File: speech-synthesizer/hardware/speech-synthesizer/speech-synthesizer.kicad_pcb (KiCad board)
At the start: 2 copper layers, 50.1 x 5.8 mm, 33 parts, among them J1 AudioJack3, Q1 BS250, U1 TMS5220C, U2 ATF22V10C, U3 74HCT245, U4 74HCT374, U5 74HCT374, U6 74HCT74, U7 74HCT688, U8 74HCT688

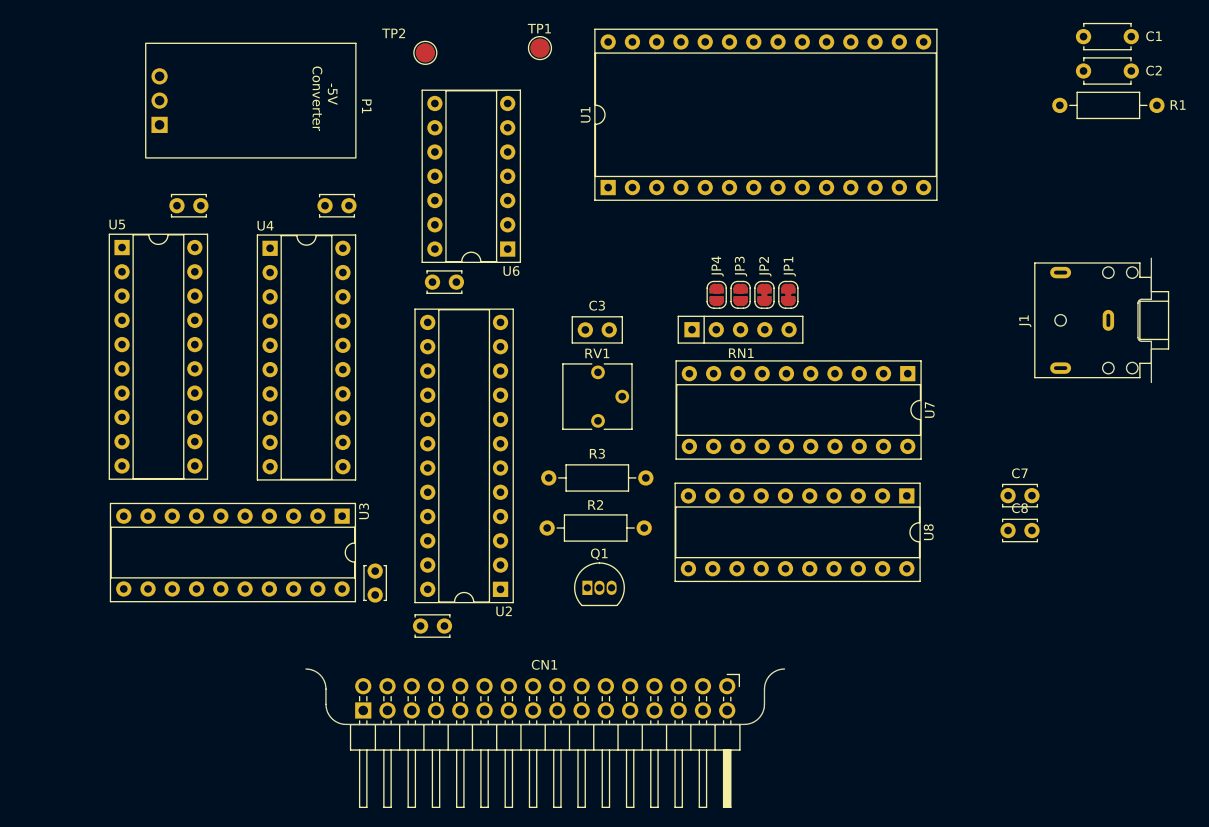
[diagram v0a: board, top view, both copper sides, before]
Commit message: created speech pcb
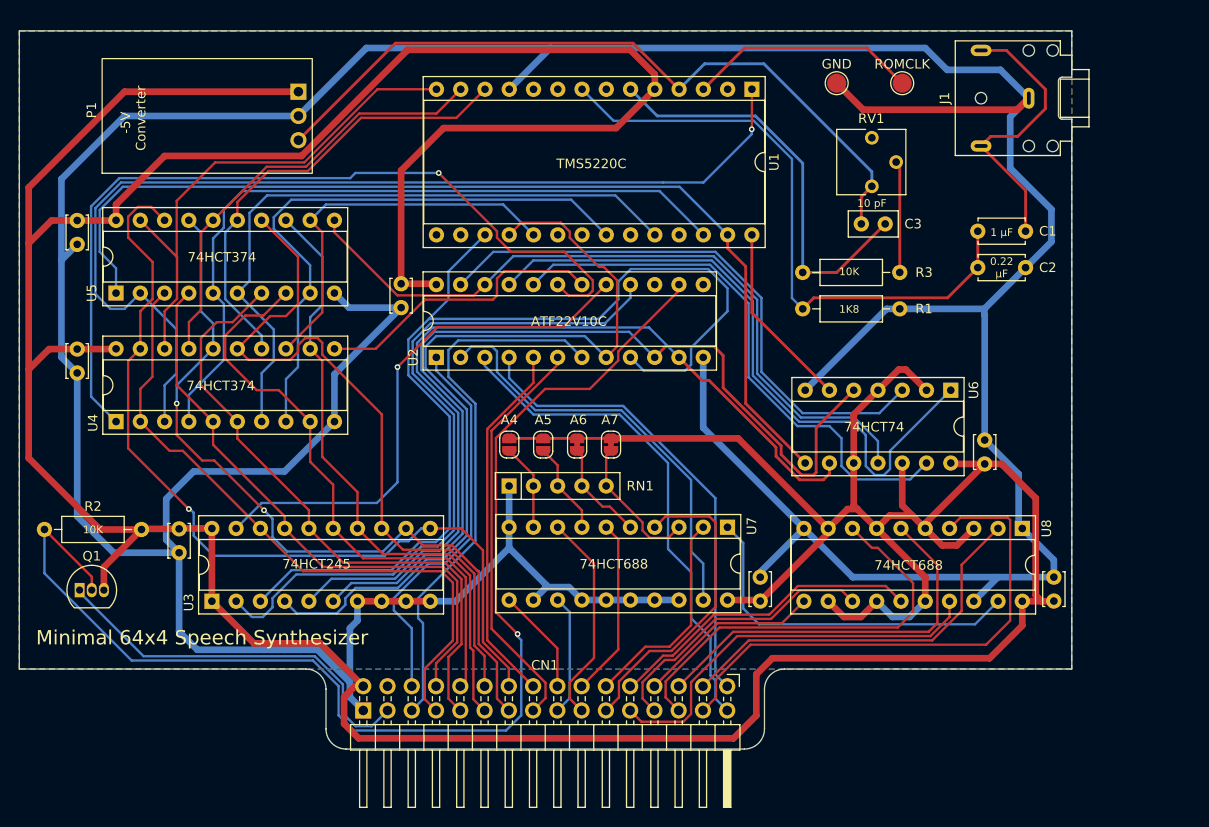
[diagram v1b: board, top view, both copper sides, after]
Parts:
- removed TP1, TP2: TestPoint, TestPoint:TestPoint_Pad_D2.0mm
- added GND: TestPoint, TestPoint:TestPoint_Pad_D2.0mm, F.Cu at (154.6, 74.7)
- added ROMCLK: TestPoint, TestPoint:TestPoint_Pad_D2.0mm, F.Cu at (161.4, 74.7)
- moved C8 86.8 mm to (85.7, 123.8), turned to 90 degrees
- moved C4 73.3 mm to (170.1, 112.0), turned to -90 degrees
- moved C7 66.5 mm to (109.0, 98.2), turned to 90 degrees
- moved C10 64.0 mm to (177.3, 126.4), turned to -90 degrees
- moved Q1 53.1 mm to (75.3, 127.7)
- moved R2 52.6 mm to (71.6, 121.4)
- moved U6 48.7 mm to (166.5, 106.8), turned to -90 degrees
- moved C6 40.8 mm to (75.1, 105.0), turned to 90 degrees
- moved C9 40.3 mm to (146.6, 126.4)
- moved RV1 37.7 mm to (158.2, 85.5)
- moved R1 34.3 mm to (151.0, 98.3)
- moved R3 34.2 mm to (151.0, 94.5)
- moved C3 30.9 mm to (157.1, 89.4)
- moved JP4 26.8 mm to (120.3, 112.5)
- moved JP3 25.9 mm to (123.8, 112.5)
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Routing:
- net +5V: track 0.00 -> 492.2 mm
- net GND: track 0.00 -> 466.6 mm
- net /~{INH}: track 0.00 -> 129.0 mm, vias 0 -> 1
- net /~{INT}: track 0.00 -> 110.9 mm
- net Net-(U1-D7): track 0.00 -> 107.2 mm, vias 0 -> 1
- net /~{WS}: track 0.00 -> 105.5 mm
- net /RS: track 0.00 -> 100.0 mm
- net /WS: track 0.00 -> 92.6 mm
- net /BUS7: track 0.00 -> 91.9 mm, vias 0 -> 1
- net /~{READY}: track 0.00 -> 88.5 mm
- net /~{STATUSo}: track 0.00 -> 88.1 mm, vias 0 -> 1
- net /BUS6: track 0.00 -> 81.6 mm, vias 0 -> 2
- net -5V: track 0.00 -> 77.9 mm
- net Net-(U1-D6): track 0.00 -> 77.5 mm
- net /WS_CLK: track 0.00 -> 77.5 mm
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- added copper zone on F.Cu, net +5V
- added copper zone on B.Cu, net GND
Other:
- board size 50.1 x 5.8 mm -> 110.2 x 75.2 mm
- board text added: "0.22 µF"
- board text added: "1 µF"
- board text added: "10 pF"
- board text added: "10K"
- board text added: "1K8"
- board text added: "74HCT245"
- board text added: "74HCT374"
- board text added: "74HCT688"
- board text added: "74HCT74"
- board text added: "A4"
- board text added: "A5"
- board text added: "A6"
- board text added: "A7"
- board text added: "ATF22V10C"
- board text added: "Minimal 64x4 Speech Synthesizer"
- board text added: "TMS5220C"

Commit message: updated documentation
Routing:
- net GND: track 466.6 -> 556.1 mm
- net /BUS6: track 81.6 -> 71.1 mm, vias 2 -> 1
- net /BUS3: track 62.0 -> 61.4 mm
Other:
- board text added: "To Back -->"
- board text added: "Trim ROMCLK to 160 KHz"
- board text added: "v1.0 by Michael Kanmprath"
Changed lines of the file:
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@@
 		)
 	)
+	(gr_text "v1.0 by Michael Kanmprath"
+		(at 70.866 134.747 0)
+		(layer "F.SilkS")
+		(effects
+			(font
+				(size 1 1)
+				(thickness 0.1)
+			)
+			(justify left bottom)
+		)
+	)
 	(gr_text "74HCT688"
 		(at 127.635 125.603 0)
@@
 		)
 	)
+	(gr_text "Trim ROMCLK\nto 160 KHz"
+		(at 153.67 82.931 90)
+		(layer "F.SilkS")
+		(effects
+			(font
+				(size 0.8 0.8)
+				(thickness 0.1)
+			)
+			(justify bottom)
+		)
+	)
+	(gr_text "To Back -->"
+		(at 169.545 134.747 0)
+		(layer "F.SilkS")
+		(effects
+			(font
+				(size 0.8 0.8)
+				(thickness 0.1)
+			)
+			(justify left bottom)
+		)
+	)
 	(gr_text "ATF22V10C"
 		(at 122.555 100.203 0)
@@
 	)
 	(gr_text "Minimal 64x4 Speech Synthesizer"
-		(at 70.739 133.604 0)
+		(at 70.739 132.969 0)
 		(layer "F.SilkS")
 		(effects
@@
 	)
 	(segment
+		(start 146.177 136.652)
+		(end 148.209 134.62)
+		(width 0.3)
+		(layer "B.Cu")
+		(net 3)
+	)
+	(segment
 		(start 105.328 70.993)
 		(end 98.216 78.105)
@@
 	)
 	(segment
+		(start 105 140.34)
+		(end 106.2 139.14)
+		(width 0.3)
+		(layer "B.Cu")
+		(net 3)
+	)
+	(segment
 		(start 174.672 76.247)
 		(end 171.704 73.279)
@@
 	)
 	(segment
+		(start 109.774943 141.732)
+		(end 115.824 141.732)
+		(width 0.3)
+		(layer "B.Cu")
+		(net 3)
+	)
+	(segment
 		(start 177.038 87.884)
 		(end 172.72 83.566)
@@
 	)
 	(segment
+		(start 148.209 134.62)
+		(end 171.958 134.62)
+		(width 0.3)
+		(layer "B.Cu")
+		(net 3)
+	)
+	(segment
 		(start 170.053 98.933)
 		(end 170.053 112.034)
@@
 	)
 	(segment
+		(start 138.049 132.334)
+		(end 139.319 133.604)
+		(width 0.3)
+		(layer "B.Cu")
+		(net 3)
+	)
+	(segment
 		(start 108.966 98.171)
 		(end 101.986 105.151)
@@
 	)
 	(segment
+		(start 139.319 133.604)
+		(end 139.319 141.097)
+		(width 0.3)
+		(layer "B.Cu")
+		(net 3)
+	)
+	(segment
 		(start 166.116 73.279)
 		(end 163.83 70.993)
@@
 	)
 	(segment
+		(start 146.177 140.589)
+		(end 146.177 136.652)
+		(width 0.3)
+		(layer "B.Cu")
+		(net 3)
+	)
+	(segment
 		(start 174.331 93.98)
 		(end 177.038 91.273)
@@
 	)
 	(segment
+		(start 175.641 130.937)
+		(end 175.641 128.036)
+		(width 0.3)
+		(layer "B.Cu")
+		(net 3)
+	)
+	(segment
 		(start 140.589 110.744)
 		(end 151.13 121.285)
@@
 	)
 	(segment
+		(start 139.319 141.097)
+		(end 140.081 141.859)
+		(width 0.3)
+		(layer "B.Cu")
+		(net 3)
+	)
+	(segment
 		(start 177.292 124.587)
 		(end 173.99 121.285)
@@
 	)
 	(segment
+		(start 108.74 140.697057)
+		(end 108.74 139.601)
+		(width 0.3)
+		(layer "B.Cu")
+		(net 3)
+	)
+	(segment
 		(start 173.609 120.904)
 		(end 173.609 115.59)
@@
 	)
 	(segment
+		(start 106.2 139.14)
+		(end 108.279 139.14)
+		(width 0.3)
+		(layer "B.Cu")
+		(net 3)
+	)
+	(segment
+		(start 144.907 141.859)
+		(end 146.177 140.589)
+		(width 0.3)
+		(layer "B.Cu")
+		(net 3)
+	)
+	(segment
+		(start 116.459 141.097)
+		(end 116.459 133.35)
+		(width 0.3)
+		(layer "B.Cu")
+		(net 3)
+	)
+	(segment
 		(start 177.292 126.385)
 		(end 177.292 124.587)
@@
 	)
 	(segment
+		(start 140.081 141.859)
+		(end 144.907 141.859)
+		(width 0.3)
+		(layer "B.Cu")
+		(net 3)
+	)
+	(segment
 		(start 132.969 128.778)
 		(end 130.429 128.778)
@@
 	)
 	(segment
+		(start 116.459 133.35)
+		(end 112.014 128.905)
+		(width 0.3)
+		(layer "B.Cu")
+		(net 3)
+	)
+	(segment
+		(start 108.74 139.601)
+		(end 108.279 139.14)
+		(width 0.3)
+		(layer "B.Cu")
+		(net 3)
+	)
+	(segment
 		(start 103.505 98.171)
 		(end 101.981 96.647)
@@
 	)
 	(segment
+		(start 115.824 141.732)
+		(end 116.459 141.097)
+		(width 0.3)
+		(layer "B.Cu")
+		(net 3)
+	)
+	(segment
 		(start 73.406 93.198)
 		(end 73.406 84.709)
@@
 	)
 	(segment
+		(start 108.74 140.697057)
+		(end 109.774943 141.732)
+		(width 0.3)
+		(layer "B.Cu")
+		(net 3)
+	)
+	(segment
+		(start 171.958 134.62)
+		(end 175.641 130.937)
+		(width 0.3)
+		(layer "B.Cu")
+		(net 3)
+	)
+	(segment
 		(start 151.13 121.285)
 		(end 156.23 126.385)
@@
 	)
 	(segment
+		(start 175.641 128.036)
+		(end 177.292 126.385)
+		(width 0.3)
+		(layer "B.Cu")
+		(net 3)
+	)
+	(segment
+		(start 138.049 128.778)
+		(end 138.049 132.334)
+		(width 0.3)
+		(layer "B.Cu")
+		(net 3)
+	)
+	(segment
 		(start 126.539 127.428)
 		(end 124.159 127.428)
@@
 	)
 	(segment
-		(start 118.999 139.099)
-		(end 118.999 135.291792)
+		(start 89.286 102.479)
+		(end 89.286 104.78)
 		(width 0.25)
 		(layer "F.Cu")
@@
 	)
 	(segment
-		(start 85.471 111.506)
-		(end 85.471 108.204)
+		(start 118.999 139.099)
+		(end 118.999 135.291792)
 		(width 0.25)
 		(layer "F.Cu")
@@
 	)
 	(segment
-		(start 94.615 119.38)
-		(end 89.408 114.173)
+		(start 93.091 108.585)
+		(end 93.091 111.887)
 		(width 0.25)
 		(layer "F.Cu")
@@
 	)
 	(segment
-		(start 89.408 114.173)
-		(end 88.138 114.173)
+		(start 93.091 111.887)
+		(end 100.838 119.634)
 		(width 0.25)
 		(layer "F.Cu")
@@
 	)
 	(segment
-		(start 88.138 114.173)
-		(end 85.471 111.506)
+		(start 89.286 104.78)
+		(end 93.091 108.585)
 		(width 0.25)
 		(layer "F.Cu")
@@
 	)
 	(via
-		(at 94.615 119.38)
-		(size 0.6)
-		(drill 0.3)
-		(layers "F.Cu" "B.Cu")
-		(net 18)
-	)
-	(via
-		(at 85.471 108.204)
+		(at 100.838 119.634)
 		(size 0.6)
 		(drill 0.3)
@@
 	)
 	(segment
-		(start 95.504 122.174)
-		(end 95.504 120.269)
-		(width 0.25)
-		(layer "B.Cu")
-		(net 18)
-	)
-	(segment
-		(start 85.471 108.204)
-		(end 85.471 106.294)
-		(width 0.25)
-		(layer "B.Cu")
-		(net 18)
-	)
-	(segment
 		(start 88.011 98.552)
 		(end 88.011 90.297)
@@
 	)
 	(segment
-		(start 89.286 102.479)
-		(end 89.286 99.827)
-		(width 0.25)
-		(layer "B.Cu")
-		(net 18)
-	)
-	(segment
-		(start 109.474 121.285)
-		(end 107.061 123.698)
-		(width 0.25)
-		(layer "B.Cu")
-		(net 18)
-	)
-	(segment
-		(start 95.504 120.269)
-		(end 94.615 119.38)
+		(start 100.838 119.634)
+		(end 107.823 119.634)
 		(width 0.25)
 		(layer "B.Cu")
@@
 	)
 	(segment
-		(start 107.061 123.698)
-		(end 97.028 123.698)
+		(start 89.286 102.479)
+		(end 89.286 99.827)
 		(width 0.25)
 		(layer "B.Cu")
@@
 	)
 	(segment
-		(start 85.471 106.294)
-		(end 89.286 102.479)
-		(width 0.25)
-		(layer "B.Cu")
-		(net 18)
-	)
-	(segment
-		(start 97.028 123.698)
-		(end 95.504 122.174)
+		(start 107.823 119.634)
+		(end 109.474 121.285)
 		(width 0.25)
 		(layer "B.Cu")
@@
 	)
 	(segment
-		(start 90.551 101.093396)
-		(end 92.647198 98.997198)
+		(start 94.550802 98.997198)
+		(end 93.716811 98.997198)
+		(width 0.25)
+		(layer "F.Cu")
+		(net 31)
+	)
+	(segment
+		(start 93.716811 98.997198)
+		(end 90.551 102.163009)
 		(width 0.25)
 		(layer "F.Cu")
@@
 	)
 	(segment
+		(start 90.551 102.163009)
+		(end 90.551 103.505)
+		(width 0.25)
+		(layer "F.Cu")
+		(net 31)
+	)
+	(segment
 		(start 94.550802 98.997198)
 		(end 96.901 96.647)
@@
 	)
 	(segment
-		(start 92.647198 98.997198)
-		(end 94.550802 98.997198)
-		(width 0.25)
-		(layer "F.Cu")
-		(net 31)
-	)
-	(segment
 		(start 101.854 121.285)
 		(end 101.854 116.713)
@@
 		(width 0.25)
 		(layer "F.Cu")
-		(net 31)
-	)
-	(segment
-		(start 90.551 103.505)
-		(end 90.551 101.093396)
-		(width 0.25)
-		(layer "F.Cu")

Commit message: update speech pld file and more
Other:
- board text added: "JLCJLCJLCJLC"
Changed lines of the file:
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@@
 			(outputformat 1)
 			(mirror no)
-			(drillshape 1)
+			(drillshape 0)
 			(scaleselection 1)
-			(outputdirectory "")
+			(outputdirectory "gerbers_v1")
 		)
 	)
@@
 		(layer "Edge.Cuts")
 	)
+	(gr_text "JLCJLCJLCJLC"
+		(at 176.022 133.985 0)
+		(layer "B.SilkS")
+		(effects
+			(font
+				(size 1 1)
+				(thickness 0.1)
+			)
+			(justify left bottom mirror)
+		)
+	)
 	(gr_text "10K"

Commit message: improved backplane
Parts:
- removed Q1: BS250, Package_TO_SOT_THT:TO-92_Inline
- removed R2: 10K, Resistor_THT:R_Axial_DIN0207_L6.3mm_D2.5mm_P10.16mm_Horizontal
- renumbered ROMCLK to TP1, GND to TP2
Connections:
- U2 pad 14: /~{INH} -> /INH
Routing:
- net /~{INH}: track 129.0 -> 0.00 mm, vias 1 -> 0
- net /INH: track 40.7 -> 72.4 mm, vias 0 -> 1
- net +5V: track 492.2 -> 484.3 mm
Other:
- board text added: "v1.1 by Michael Kanmprath"
- board text removed: "v1.0 by Michael Kanmprath"

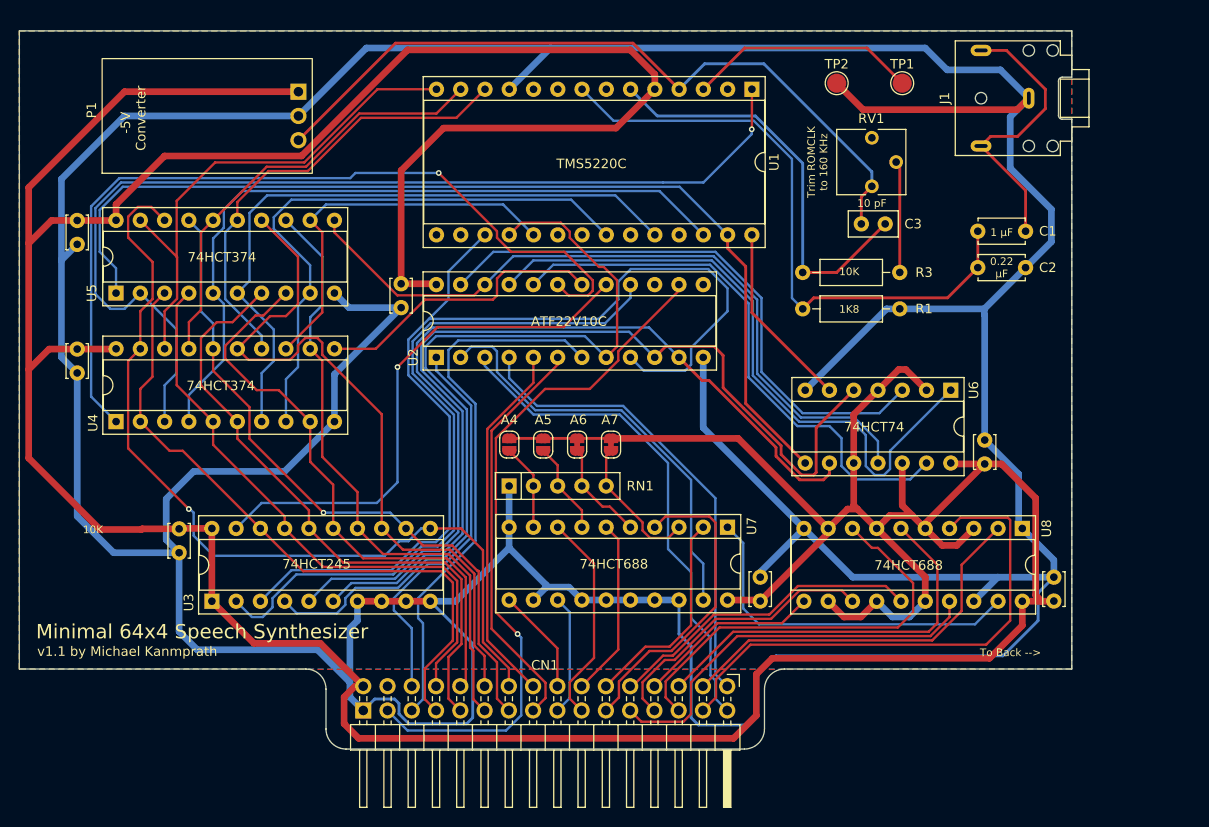
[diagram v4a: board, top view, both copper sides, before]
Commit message: improved silkscreen
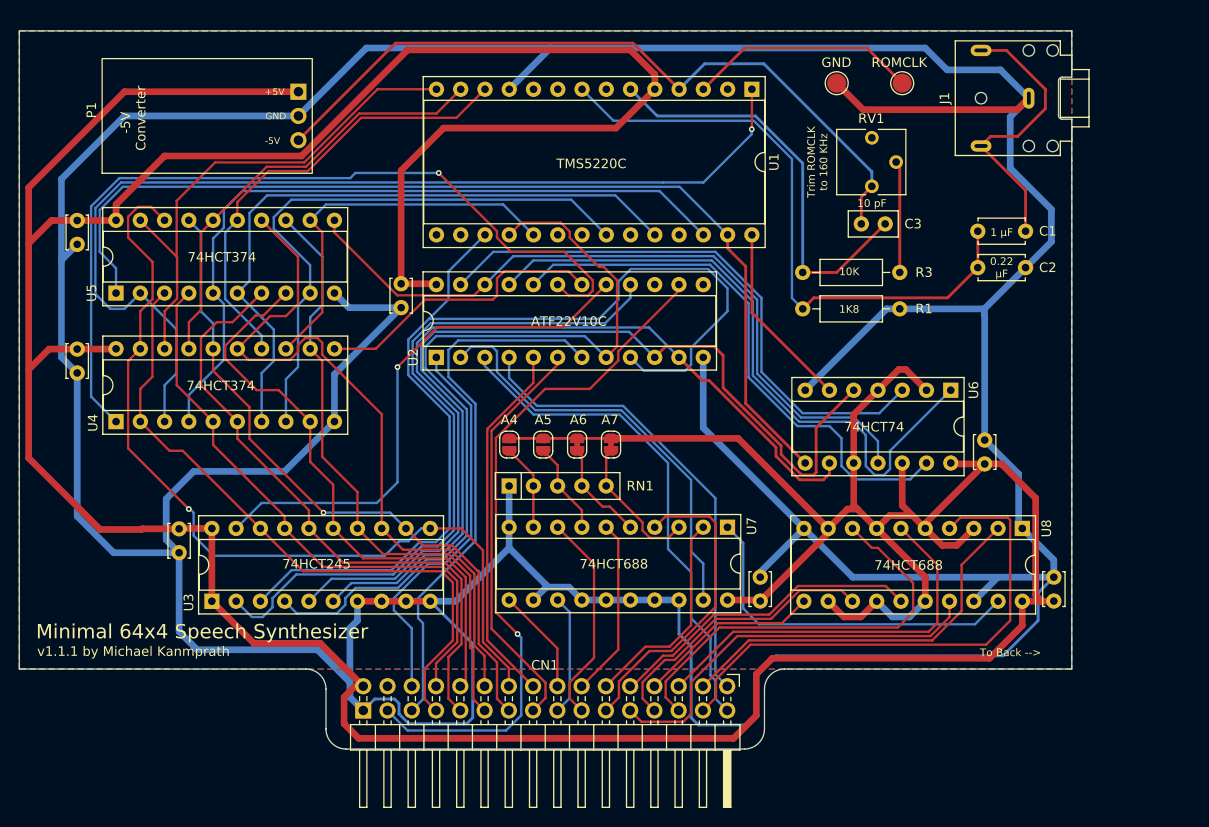
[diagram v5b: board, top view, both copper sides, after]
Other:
- board text added: "+5V"
- board text added: "-5V"
- board text added: "GND"
- board text added: "ROMCLK"
- board text added: "v1.1.1 by Michael Kanmprath"
- board text removed: "v1.1 by Michael Kanmprath"
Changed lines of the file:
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@@
 			(at 0 -1.998 0)
 			(layer "F.SilkS")
+			(hide yes)
 			(effects
 				(font
@@
 			(at 0 -1.998 0)
 			(layer "F.SilkS")
+			(hide yes)
 			(effects
 				(font
@@
 		)
 	)
+	(gr_text "+5V"
+		(at 94.6912 75.9968 0)
+		(layer "F.SilkS")
+		(effects
+			(font
+				(size 0.7 0.7)
+				(thickness 0.1)
+			)
+			(justify left bottom)
+		)
+	)
 	(gr_text "10K"
 		(at 154.813 94.869 0)
@@
 		)
 	)
-	(gr_text "10K"
-		(at 76.708 121.412 0)
-		(layer "F.SilkS")
-		(effects
-			(font
-				(size 0.8 0.8)
-				(thickness 0.1)
-			)
-		)
-	)
 	(gr_text "10 pF"
 		(at 158.242 87.249 0)
@@
 		)
 	)
-	(gr_text "v1.1 by Michael Kanmprath"
+	(gr_text "v1.1.1 by Michael Kanmprath"
 		(at 70.866 134.747 0)
 		(layer "F.SilkS")
@@
 		)
 	)
+	(gr_text "GND"
+		(at 152.9588 73.1 0)
+		(layer "F.SilkS")
+		(effects
+			(font
+				(size 1 1)
+				(thickness 0.15)
+			)
+			(justify left bottom)
+		)
+	)
+	(gr_text "GND"
+		(at 94.742 78.5368 0)
+		(layer "F.SilkS")
+		(effects
+			(font
+				(size 0.7 0.7)
+				(thickness 0.1)
+			)
+			(justify left bottom)
+		)
+	)
 	(gr_text "74HCT245"
 		(at 96.52 125.603 0)
@@
 		)
 	)
+	(gr_text "ROMCLK"
+		(at 158.1912 73.1 0)
+		(layer "F.SilkS")
+		(effects
+			(font
+				(size 1 1)
+				(thickness 0.15)
+			)
+			(justify left bottom)
+		)
+	)
 	(gr_text "74HCT74"
 		(at 155.321 111.252 0)
@@
 			)
 			(justify left bottom)
+		)
+	)
+	(gr_text "-5V"
+		(at 94.6912 81.1276 0)
+		(layer "F.SilkS")
+		(effects
+			(font
+				(size 0.7 0.7)
+				(thickness 0.1)
+			)
+			(justify left bottom)
